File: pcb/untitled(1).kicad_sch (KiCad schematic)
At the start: 1 part

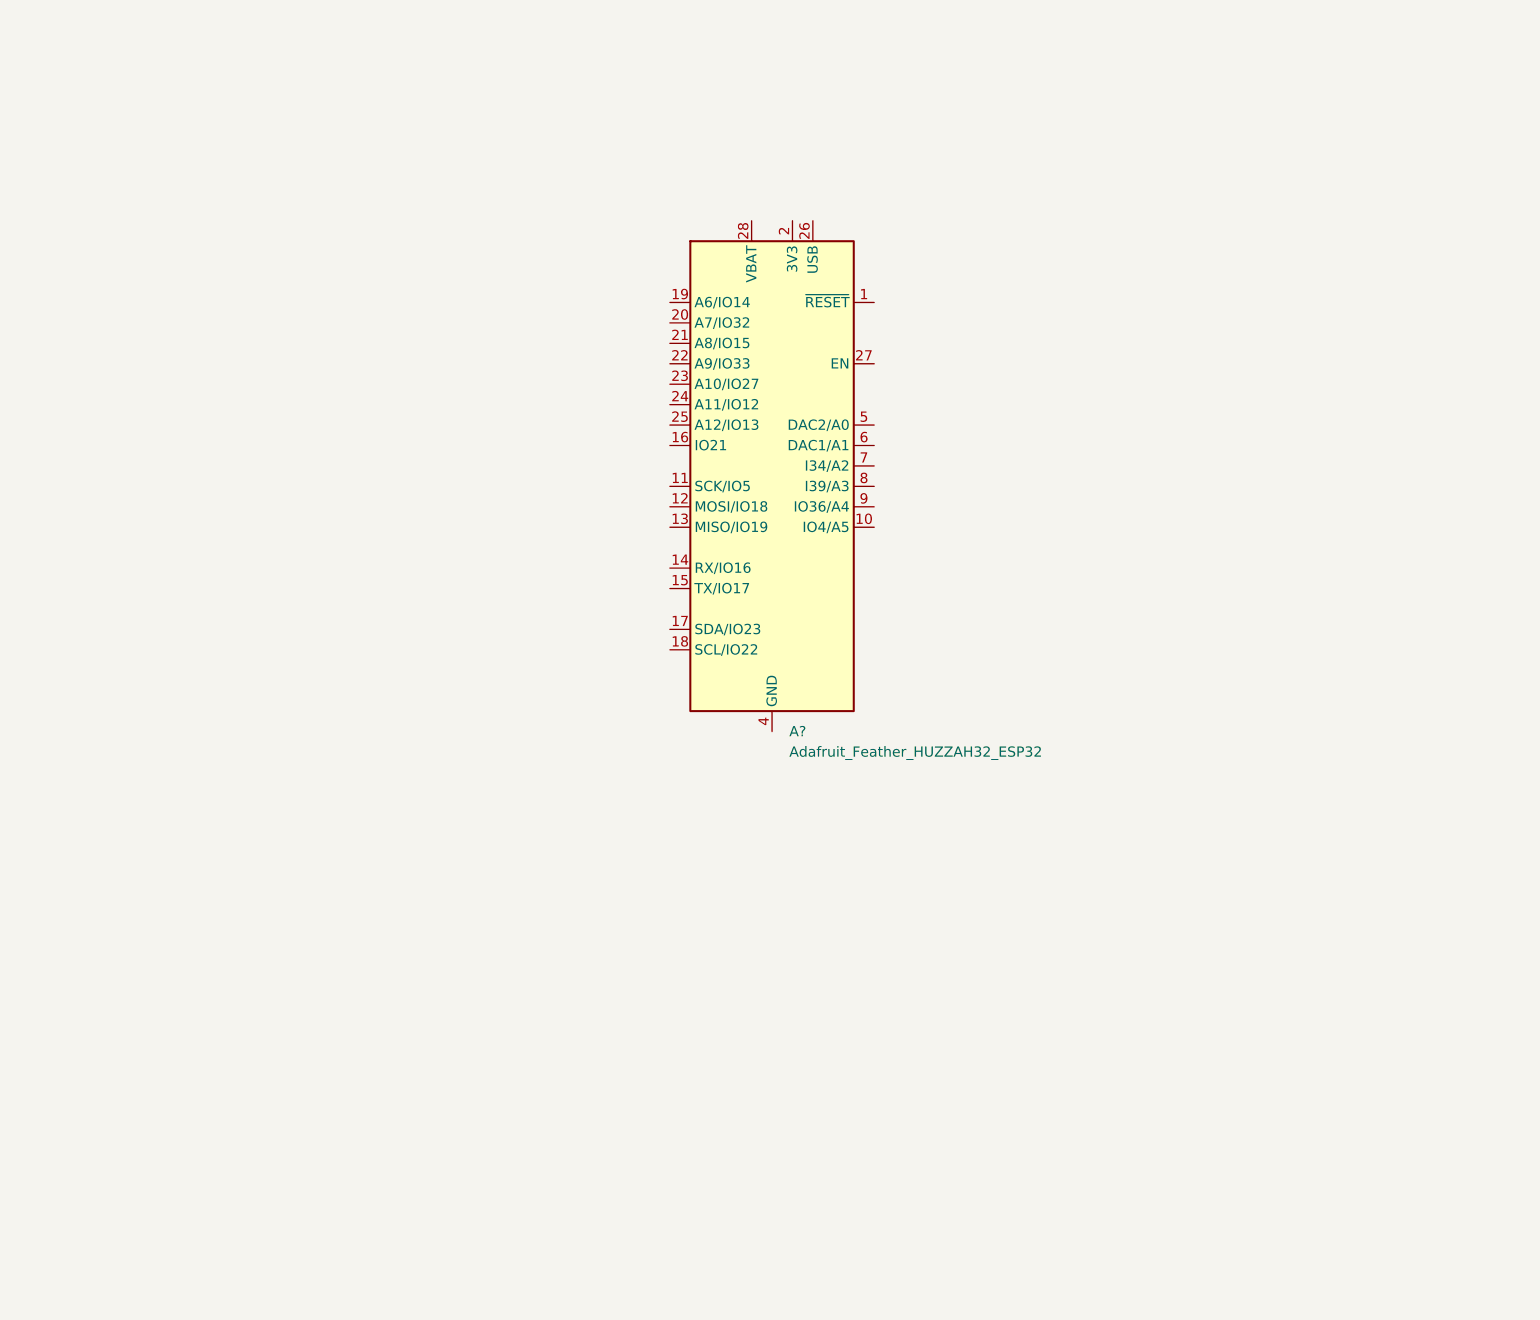
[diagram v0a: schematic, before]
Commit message: Upload of rcs controller board 1st draft
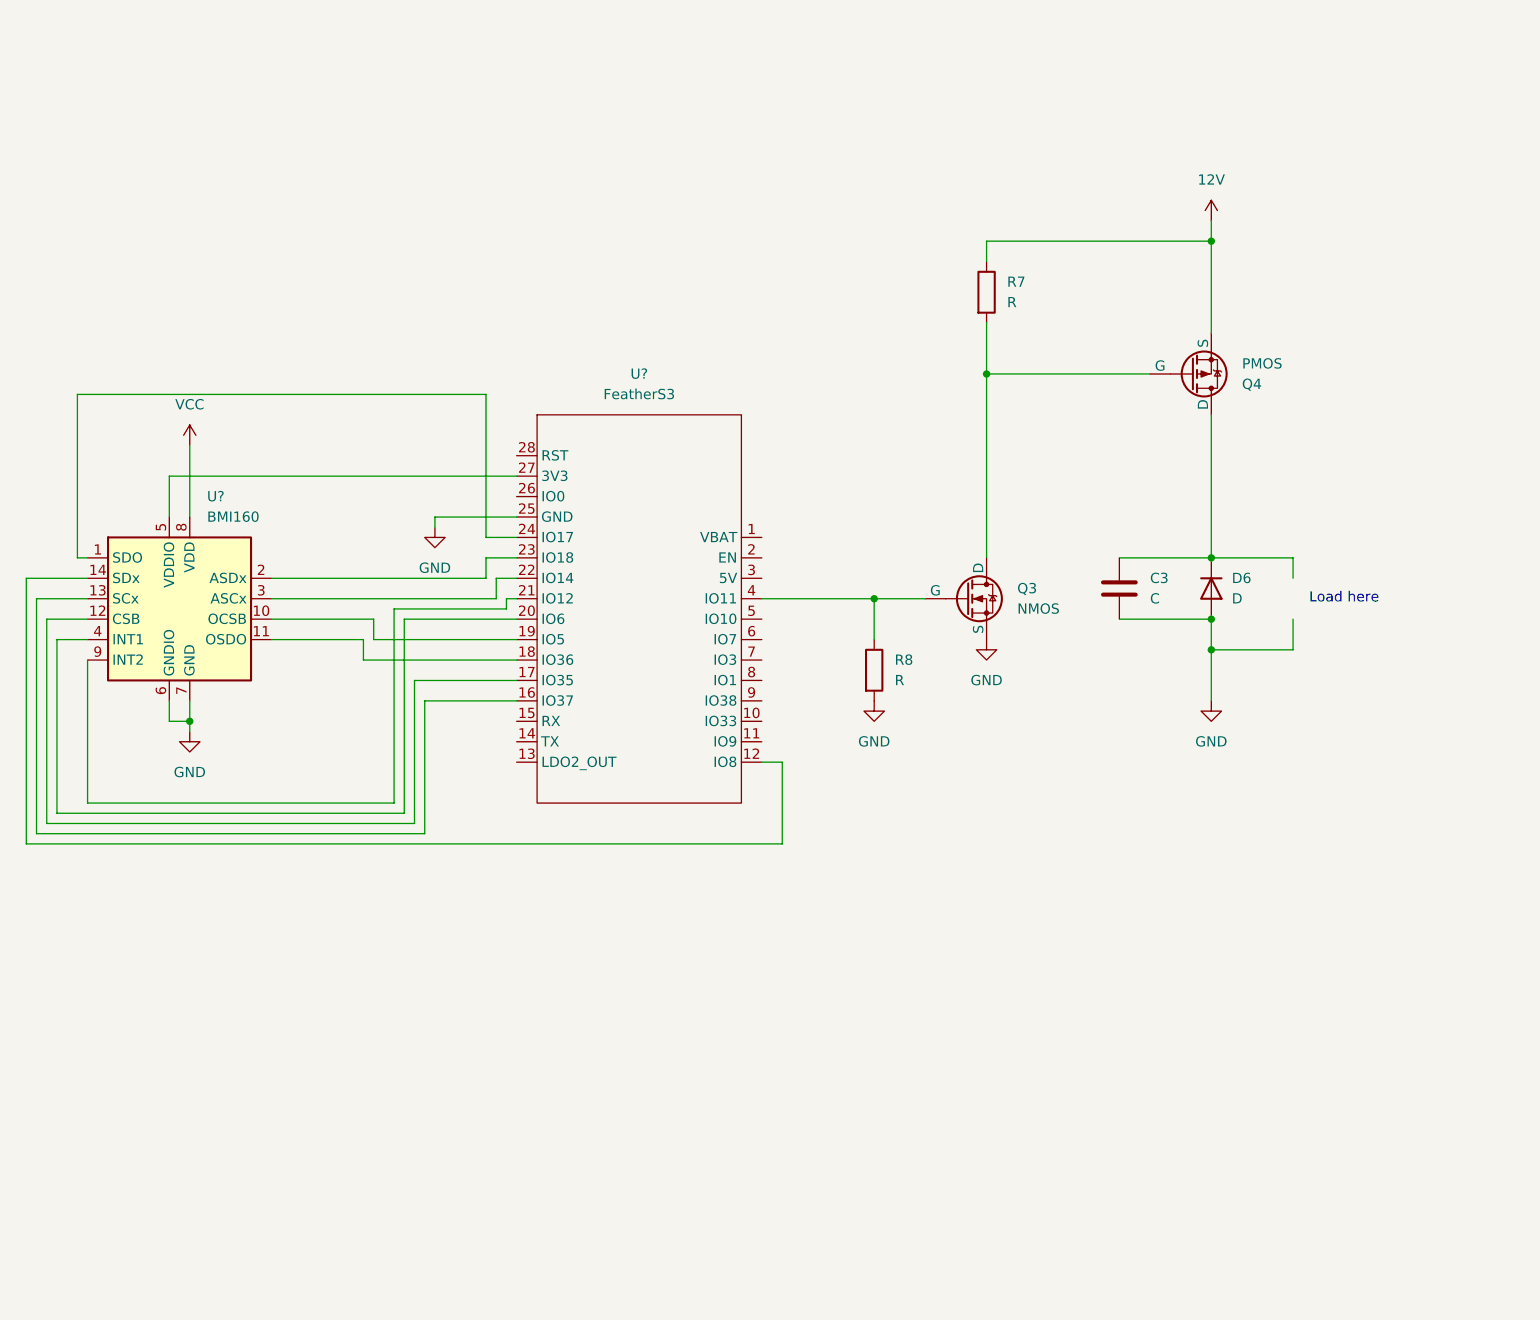
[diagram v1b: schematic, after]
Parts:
- removed A?: Adafruit_Feather_HUZZAH32_ESP32, Module:Adafruit_Feather, symbol MCU_Module:Adafruit_Feather_HUZZAH32_ESP32
- added C3: C, symbol Device:C
- added D6: D, symbol Device:D
- added Q3: NMOS, symbol Simulation_SPICE:NMOS
- added Q4: PMOS, symbol Simulation_SPICE:PMOS
- added R7, R8: R, symbol Device:R
- added U?: BMI160, Package_LGA:Bosch_LGA-14_3x2.5mm_P0.5mm, symbol Sensor_Motion:BMI160
- added U?: FeatherS3, symbol Additional_symbols:FeatherS3
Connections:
- new net: U?.1 (SDO), U?.24 (IO17)
- new net: U?.10 (OCSB), U?.19 (IO5)
- new net: U?.11 (OSDO), U?.18 (IO36)
- new net: U?.12 (CSB), U?.17 (IO35)
- new net: U?.13 (SCx), U?.16 (IO37)
- new net: U?.12 (IO8), U?.14 (SDx)
- new net: U?.2 (ASDx), U?.23 (IO18)
- new net: U?.22 (IO14), U?.3 (ASCx)
- new net: U?.20 (IO6), U?.4 (INT1)
- new net: U?.27 (3V3), U?.5 (VDDIO)
- new net: U?.21 (IO12), U?.9 (INT2)
- new net: C3.1, D6.1 (K), Q4.1 (D)
- new net: Q3.1 (D), Q4.2 (G), R7.2
- new net: Q3.2 (G), R8.1, U?.4 (IO11)
- new net 12V: Q4.3 (S), R7.1
- new net GND: C3.2, D6.2 (A), Q3.3 (S), R8.2, U?.25 (GND), U?.6 (GNDIO), U?.7 (GND)
- new net VCC: U?.8 (VDD)
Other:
- note added: "Load here"

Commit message: Updated with footprint and more fleshed out circuit
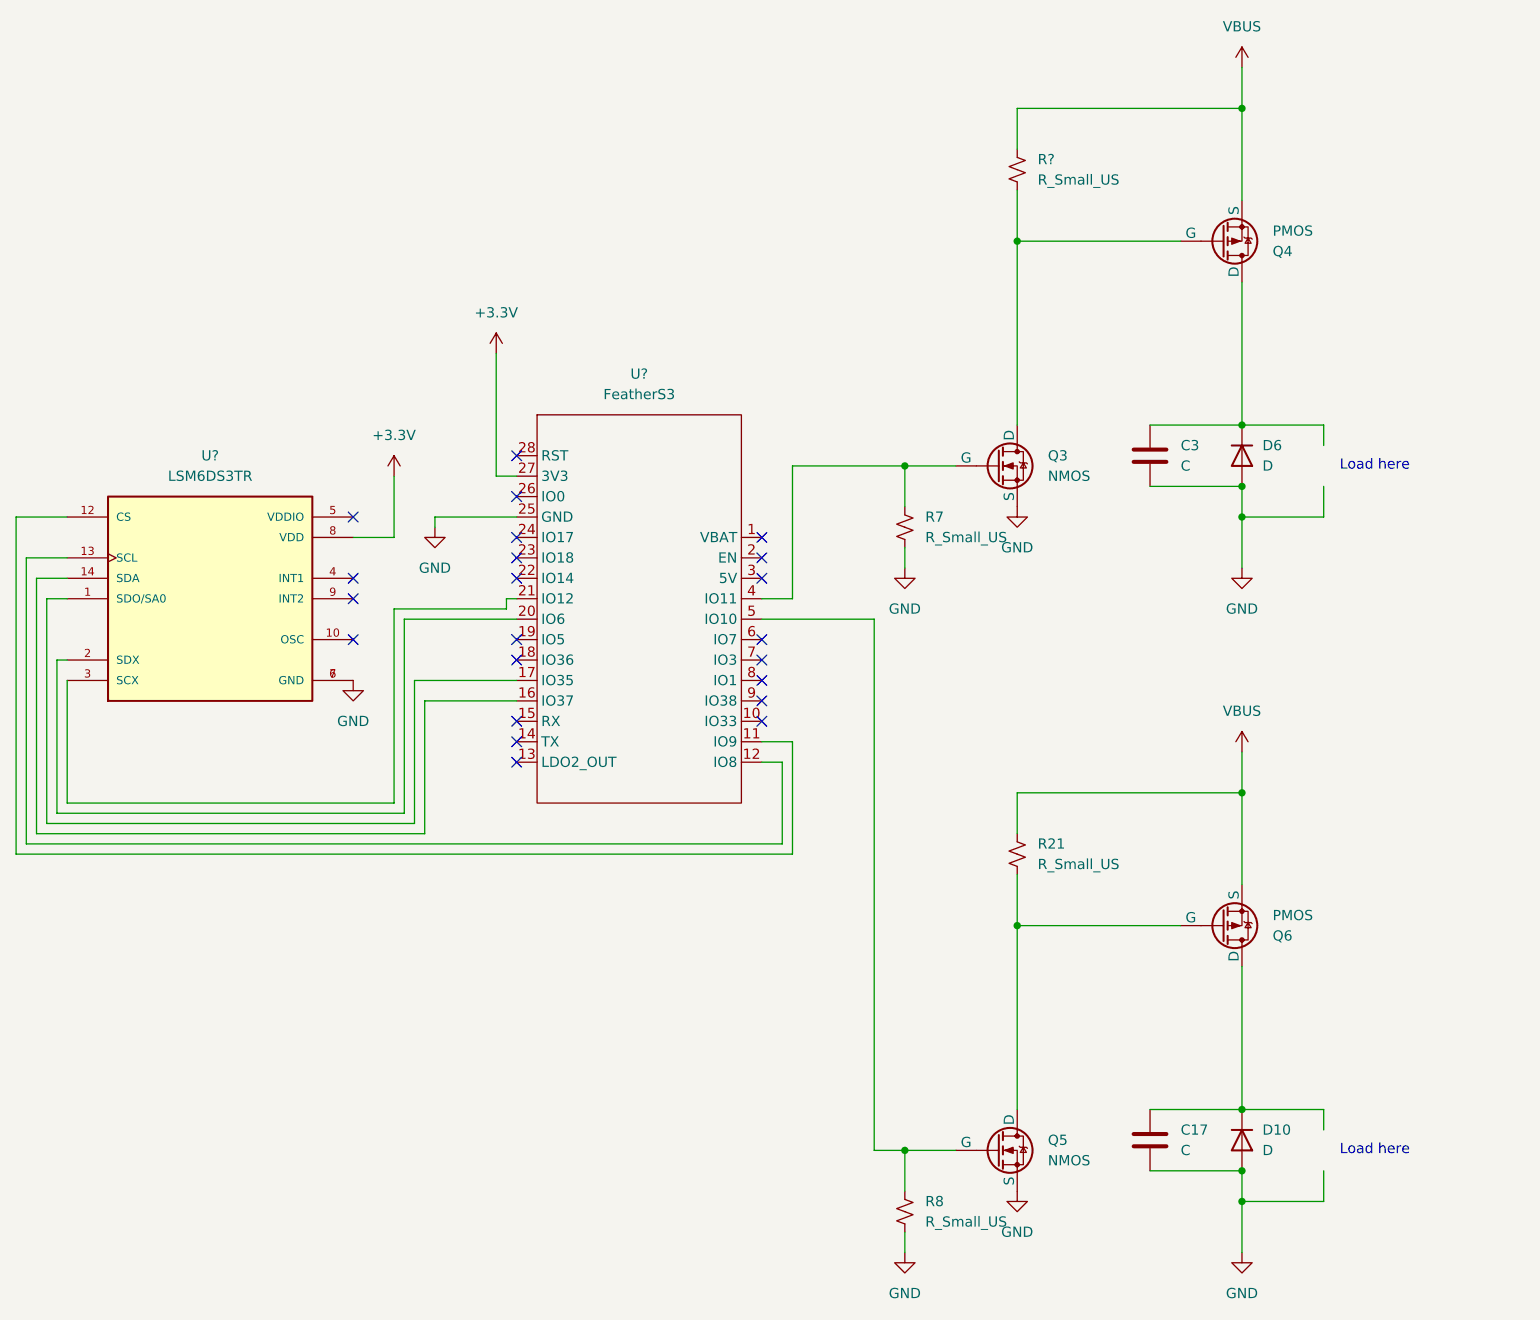
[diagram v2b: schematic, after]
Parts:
- removed R7, R8: R, symbol Device:R
- removed U?: BMI160, Package_LGA:Bosch_LGA-14_3x2.5mm_P0.5mm, symbol Sensor_Motion:BMI160
- added C17: C, symbol Device:C
- added D10: D, symbol Device:D
- added Q5: NMOS, symbol Simulation_SPICE:NMOS
- added Q6: PMOS, symbol Simulation_SPICE:PMOS
- added R21, R7, R8, R?: R_Small_US, symbol Device:R_Small_US
- added U?: LSM6DS3TR, symbol LSM6DS3TR:LSM6DS3TR
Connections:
- net GND: now also C17.2, D10.2 (A), Q5.3 (S), R7.2, R8.2, U?.6 (GND), U?.7 (GND)
- net at U?.17 (IO35): now also U?.1 (SDO/SA0)
- net at U?.16 (IO37): now also U?.14 (SDA)
- net at U?.12 (IO8): now also U?.13 (SCL)
- net at U?.20 (IO6): now also U?.2 (SDX)
- net +3.3V: now reaches U?.27 (3V3)
- net +3.3V: now also U?.8 (VDD)
- net at U?.21 (IO12): now also U?.3 (SCX)
- net at Q3.1 (D), Q4.2 (G): now also R?.2
- net at Q3.2 (G), U?.4 (IO11): now also R7.1
- net at U?.11 (IO9): now also U?.12 (CS)
- net at U?.5 (IO10): now also Q5.2 (G), R8.1
- net 12V renamed VBUS
- net VBUS: now also Q6.3 (S), R21.1, R?.1
- new net: Q5.1 (D), Q6.2 (G), R21.2
- new net: C17.1, D10.1 (K), Q6.1 (D)
- no-connect marks 0 -> 22
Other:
- title: (none) -> RCS Controller Board
- moved on the sheet: C3, D6, Q3, Q4

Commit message: Rough draft schematic, no ERC errors, ready for layout
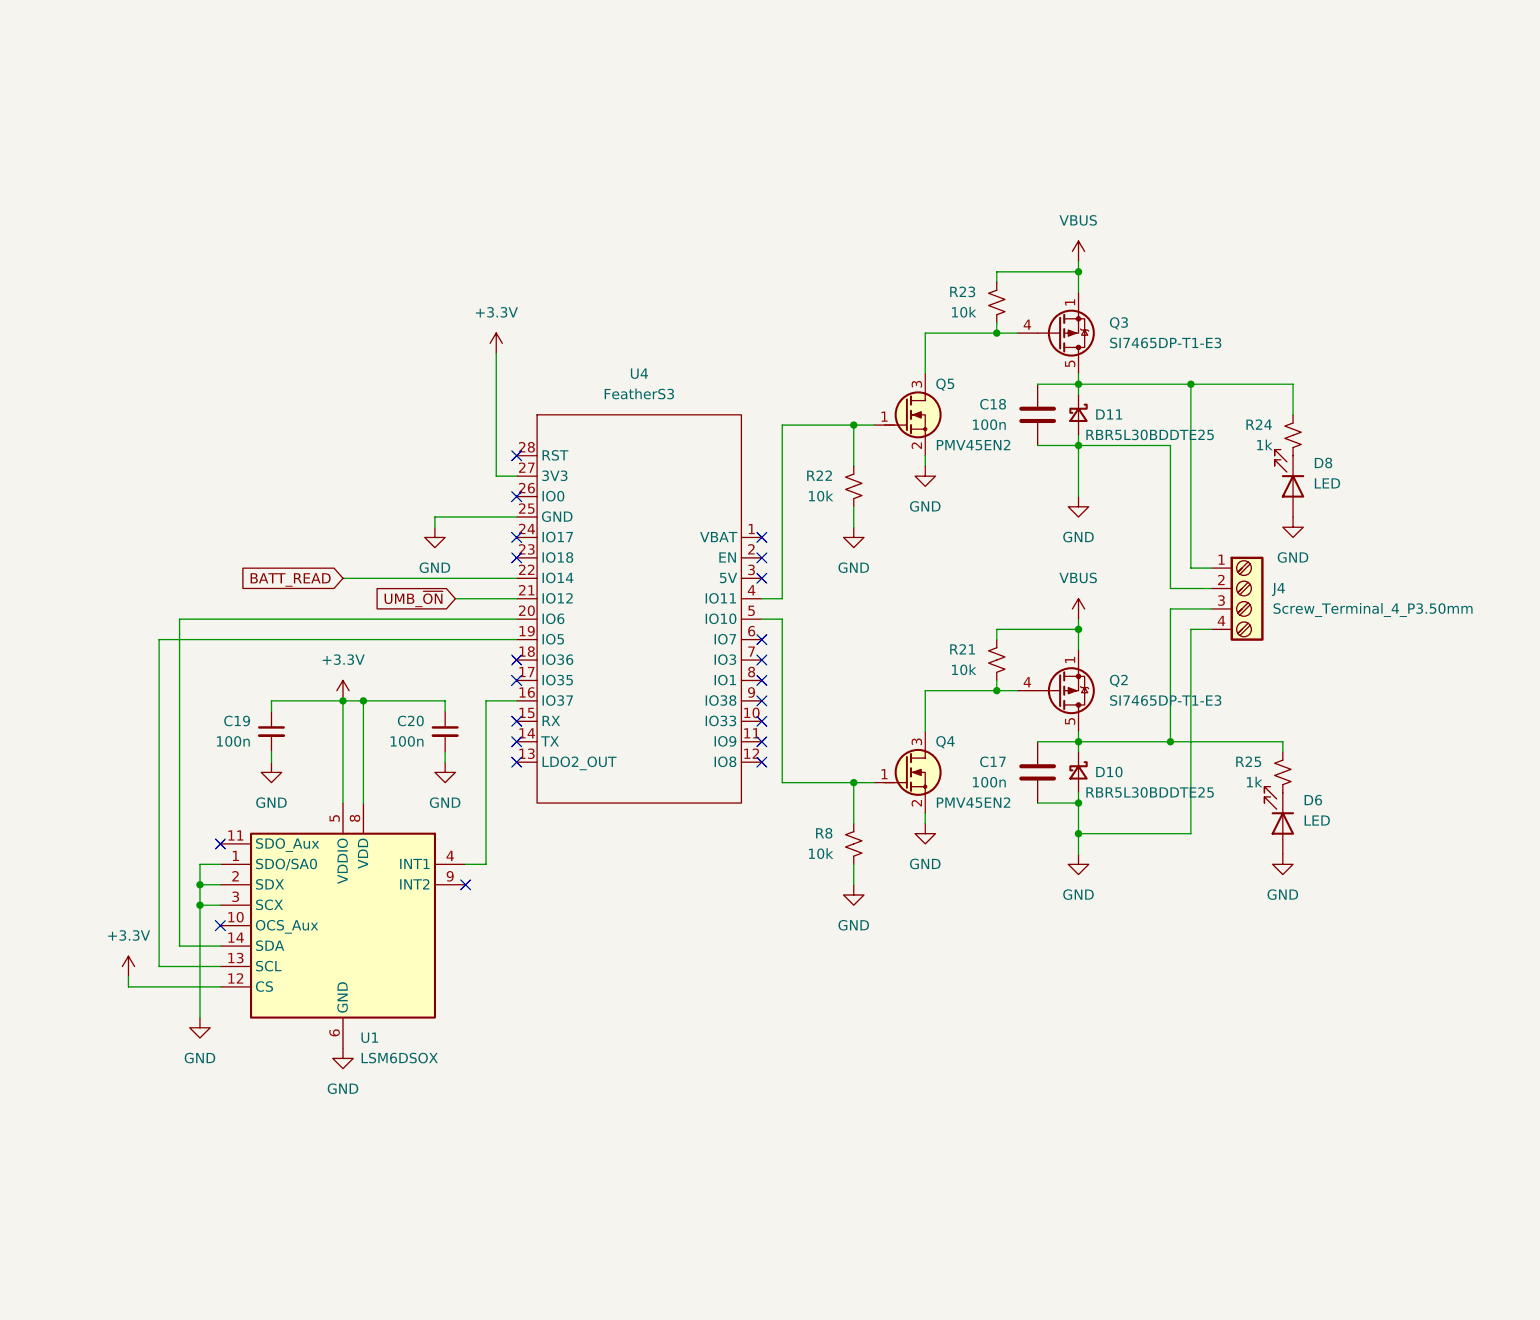
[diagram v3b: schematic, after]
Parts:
- removed C3: C, symbol Device:C
- removed D10, D6: D, symbol Device:D
- removed Q3, Q5: NMOS, symbol Simulation_SPICE:NMOS
- removed Q4, Q6: PMOS, symbol Simulation_SPICE:PMOS
- removed R7, R?: R_Small_US, symbol Device:R_Small_US
- removed U?: LSM6DS3TR, symbol LSM6DS3TR:LSM6DS3TR
- added C18: 100n, Capacitor_SMD:C_0603_1608Metric, symbol Device:C
- added C19, C20: 100n, Capacitor_SMD:C_0603_1608Metric, symbol Device:C_Small
- added D10, D11: RBR5L30BDDTE25, Diode_SMD:D_SMA, symbol Device:D_Schottky_Small
- added D6, D8: LED, LED_SMD:LED_0603_1608Metric, symbol Device:LED
- added J4: Screw_Terminal_4_P3.50mm, TerminalBlock_Phoenix:TerminalBlock_Phoenix_PT-1,5-4-3.5-H_1x04_P3.50mm_Horizontal, symbol PCM_SL_Screw_Terminal:Screw_Terminal_4_P3.50mm
- added Q2, Q3: SI7465DP-T1-E3, PCM_Package_SON_AKL:Infineon_PG-TDSON-8, symbol Transistor_FET:Si7141DP
- added Q4, Q5: PMV45EN2, PCM_Package_TO_SOT_SMD_AKL:SOT-23, symbol PCM_Transistor_MOSFET_AKL:PMV45EN2
- added R22, R23: 10k, Resistor_SMD:R_0603_1608Metric, symbol Device:R_Small_US
- added R24, R25: 1k, Resistor_SMD:R_0603_1608Metric, symbol Device:R_Small_US
- added U1: LSM6DSOX, Package_LGA:LGA-14_3x2.5mm_P0.5mm_LayoutBorder3x4y, symbol Sensor_Motion:LSM6DSM
- C17: value C -> 100n; footprint (none) -> Capacitor_SMD:C_0603_1608Metric; DPN (none) -> 1276-6854-1-ND; DST (none) -> DigiKey; MFR (none) -> Samsung Microelectronics; MPN (none) -> CL10B104KB8WPNC
- R21, R8: value R_Small_US -> 10k; footprint (none) -> Resistor_SMD:R_0603_1608Metric; MFR (none) -> Yageo; MPN (none) -> RC0603FR-0710KL
- U4: renamed from U?; footprint (none) -> Module:Adafruit_Feather
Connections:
- net +3.3V: now also C19.1, C20.1, U1.12 (CS), U1.5 (VDDIO), U1.8 (VDD)
- net GND: now also C18.2, C19.2, C20.2, D10.2 (A), D11.2 (A), D6.2 (A), D8.2 (A), J4.2, J4.4, Q4.2 (S), Q5.2 (S), R22.2, U1.1 (SDO/SA0), U1.2 (SDX), U1.3 (SCX), U1.6 (GND), U1.7 (GND)
- net VBUS: now also Q2.1 (S), Q2.2 (S), Q2.3 (S), Q3.1 (S), Q3.2 (S), Q3.3 (S), R23.1
- net at R21.2: now also Q2.4 (G), Q4.3 (D)
- net at C17.1: now also D10.1 (K), J4.3, Q2.5 (D), R25.1
- net at R8.1, U4.5 (IO10): now also Q4.1 (G)
- net at U4.16 (IO37): now also U1.4 (INT1)
- net at U4.19 (IO5): now also U1.13 (SCL)
- net at U4.20 (IO6): now also U1.14 (SDA)
- net UMB_~{ON}: now reaches U4.21 (IO12)
- net BATT_READ: now reaches U4.22 (IO14)
- net at U4.4 (IO11): now also Q5.1 (G), R22.1
- new net: D6.1 (K), R25.2
- new net: C18.1, D11.1 (K), J4.1, Q3.5 (D), R24.1
- new net: Q3.4 (G), Q5.3 (D), R23.2
- new net: D8.1 (K), R24.2
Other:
- note removed: "Load here"
- moved on the sheet: C17, R21, R8
